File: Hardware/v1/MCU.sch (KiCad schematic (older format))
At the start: 63 parts, among them J10 SERV_0, J11 SERV_1, J12 SERV_2, J13 SERV_3, J14 SERV_0, J15 SERV_1, J16 SERV_2, J17 SERV_3, J18 GPIO1, J19 GPIO2, J20 GPIO3, J21 GPIO4, J22 GPIO5, J23 GPIO6, J24 DACS, J4 SERV_0, J5 SERV_1, J6 SERV_2, J7 SERV_3, J8 CAN, J9 USB_B_Mini, P1 SWD, SW2 BOOT0, U4 BMI160, U5 STM32F405RGTx, U6 TJA1051TK-3, Y1 8Mhz

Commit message: bah
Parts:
- J15: renamed from J10; value SERV_0 -> SERV_4
- J16: renamed from J11; value SERV_1 -> SERV_5
- J17: renamed from J12; value SERV_2 -> SERV_6
- J18: renamed from J13; value SERV_3 -> SERV_7
- J21: renamed from J14; value SERV_0 -> SERV_8
- J22: renamed from J15; value SERV_1 -> SERV_9
- J23: renamed from J16; value SERV_2 -> SERV_10
- J24: renamed from J17; value SERV_3 -> SERV_11
- renumbered C30 to C29, C31 to C30, C32 to C31, C33 to C32, C34 to C33, C35 to C34, J24 to J10, J4 to J11, J5 to J12, J6 to J13, J7 to J14, J8 to J19, J9 to J20, J18 to J4, J19 to J5, J20 to J6, J21 to J7, J22 to J8, J23 to J9, R12 to R11, R13 to R12, R15 to R13, R11 to R14, R14 to R15, R20 to R18, R21 to R19, R22 to R20, R23 to R21, R18 to R22, R24 to R23, R25 to R24, R26 to R25, R27 to R26, R19 to R27
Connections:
- net GND: no longer C28.2, J11.2 (Pin_2), J12.2 (Pin_2), J13.2 (Pin_2), J14.2 (Pin_2), J15.2 (Pin_2), J16.2 (Pin_2), J17.2 (Pin_2), J18.2 (Pin_2), J19.4 (Pin_4), J21.2 (Pin_2), J22.2 (Pin_2), J23.2 (Pin_2), J24.2 (Pin_2), U5.42 (PA9), U6.3 (VCC)
- new net +5V: C28.2, J11.2 (Pin_2), J12.2 (Pin_2), J13.2 (Pin_2), J14.2 (Pin_2), J15.2 (Pin_2), J16.2 (Pin_2), J17.2 (Pin_2), J18.2 (Pin_2), J19.4 (Pin_4), J21.2 (Pin_2), J22.2 (Pin_2), J23.2 (Pin_2), J24.2 (Pin_2), U5.42 (PA9), U6.3 (VCC)

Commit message: tweaks and simplification
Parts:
- removed J21: SERV_8, Connector_PinHeader_2.54mm:PinHeader_1x03_P2.54mm_Vertical, symbol Connector:Conn_01x03_Male
- removed J22: SERV_9, Connector_PinHeader_2.54mm:PinHeader_1x03_P2.54mm_Vertical, symbol Connector:Conn_01x03_Male
- removed J23: SERV_10, Connector_PinHeader_2.54mm:PinHeader_1x03_P2.54mm_Vertical, symbol Connector:Conn_01x03_Male
- removed J24: SERV_11, Connector_PinHeader_2.54mm:PinHeader_1x03_P2.54mm_Vertical, symbol Connector:Conn_01x03_Male
- removed J7: GPIO4, Connector_JST:JST_PH_B4B-PH-K_1x04_P2.00mm_Vertical, symbol Connector:Conn_01x04_Female
- removed J8: GPIO5, Connector_JST:JST_PH_B4B-PH-K_1x04_P2.00mm_Vertical, symbol Connector:Conn_01x04_Female
- removed J9: GPIO6, Connector_JST:JST_PH_B4B-PH-K_1x04_P2.00mm_Vertical, symbol Connector:Conn_01x04_Female
- removed R23, R24, R25, R26: 220R, Resistor_SMD:R_0603_1608Metric, symbol Device:R_Small
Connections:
- net GP14 is gone; now on net IMU_INT2: U5.25 (PC5)
- net IMU_INT2: no longer U5.57 (PB5)
- net GP10: no longer names the net of U5.33 (PB12)
- net GP11: no longer names the net of U5.34 (PB13)
- net GP12: no longer names the net of U5.35 (PB14)
- net GP13: no longer names the net of U5.24 (PC4)
- net GP15: no longer names the net of U5.4 (PC15)
- net GP16: no longer names the net of U5.58 (PB6)
- net GP17: no longer names the net of U5.59 (PB7)
- net GP18: no longer names the net of U5.36 (PB15)
- net SERV10: no longer names the net of U5.38 (PC7)
- net SERV11: no longer names the net of U5.39 (PC8)
- net SERV12: no longer names the net of U5.40 (PC9)
- net SERV9: no longer names the net of U5.37 (PC6)
- no-connect marks 10 -> 23

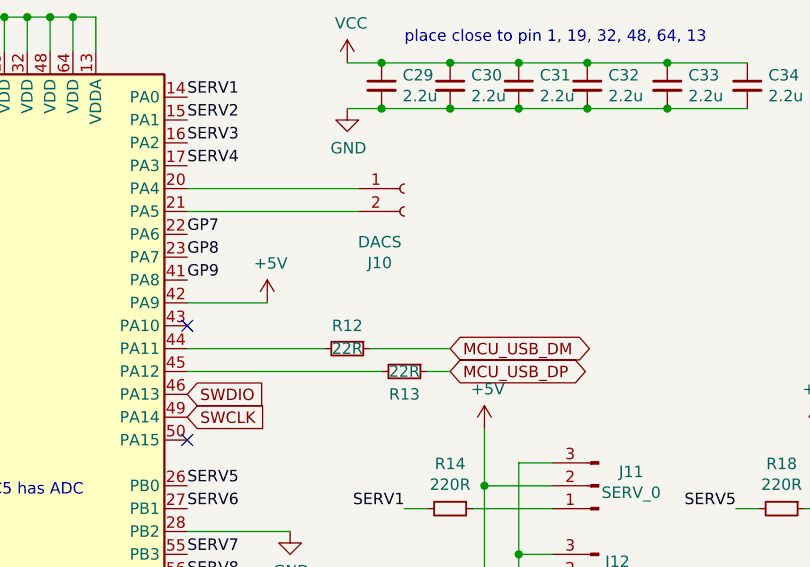
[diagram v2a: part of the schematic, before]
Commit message: adding some descriptions on F silks
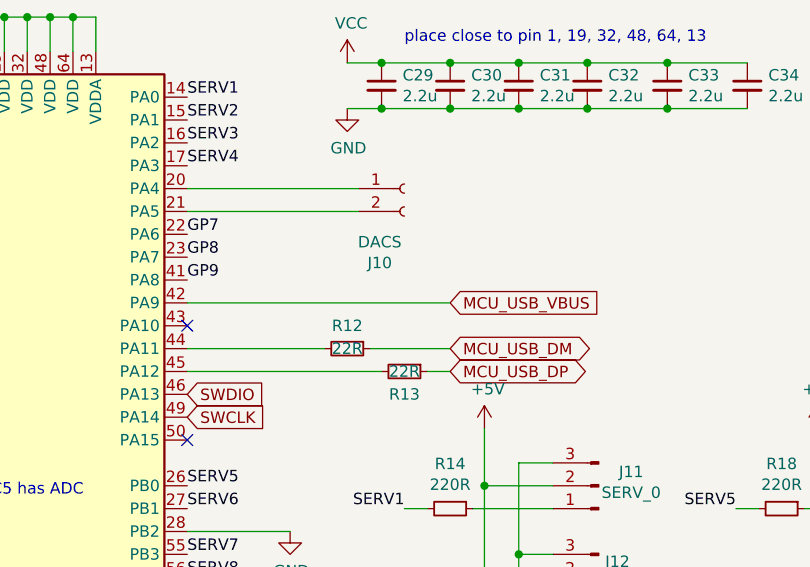
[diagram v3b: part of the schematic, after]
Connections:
- net +5V: no longer U5.42 (PA9)
- net MCU_USB_VBUS: now also U5.42 (PA9)
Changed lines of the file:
@@
 LED1
-Wire Wire Line
-	5750 2700 6100 2700
-$Comp
-L Device:R_Small R12
-U 1 1 5D93C493
-P 5650 2700
-F 0 "R12" V 5550 2700 50  0000 C CNN
-F 1 "22R" V 5650 2700 50  0000 C CNN
-F 2 "Resistor_SMD:R_0603_1608Metric" H 5650 2700 50  0001 C CNN
-F 3 "~" H 5650 2700 50  0001 C CNN
-F 4 "311-22GRCT-ND" H 5650 2700 50  0001 C CNN "OrderN"
-	1    5650 2700
-	0    1    1    0
-$EndComp
 Wire Wire Line
 	4950 2800 5800 2800
@@
 	-1   0    0    1
 $EndComp
-Wire Wire Line
-	4950 2700 5550 2700
 Wire Wire Line
 	9800 2200 10500 2200
@@
 	4900 5950 5600 5950
 $Comp
-L power:+5V #PWR034
-U 1 1 5E17915F
-P 5300 2500
-F 0 "#PWR034" H 5300 2350 50  0001 C CNN
-F 1 "+5V" H 5315 2673 50  0000 C CNN
-F 2 "" H 5300 2500 50  0001 C CNN
-F 3 "" H 5300 2500 50  0001 C CNN
-	1    5300 2500
-	1    0    0    -1
-$EndComp
-Wire Wire Line
-	4950 2500 5300 2500
-$Comp
 L power:+5V #PWR0101
 U 1 1 5E0CAA07
@@
 SDA
 NoConn ~ 4950 3800
+Text GLabel 6100 2500 2    50   Input ~ 0
+MCU_USB_VBUS
+Wire Wire Line
+	4950 2700 5550 2700
+Wire Wire Line
+	5750 2700 6100 2700
+$Comp
+L Device:R_Small R12
+U 1 1 5D93C493
+P 5650 2700
+F 0 "R12" V 5550 2700 50  0000 C CNN
+F 1 "22R" V 5650 2700 50  0000 C CNN
+F 2 "Resistor_SMD:R_0603_1608Metric" H 5650 2700 50  0001 C CNN
+F 3 "~" H 5650 2700 50  0001 C CNN
+F 4 "311-22GRCT-ND" H 5650 2700 50  0001 C CNN "OrderN"
+	1    5650 2700
+	0    1    1    0
+$EndComp
+Wire Wire Line
+	4950 2500 6100 2500
 $EndSCHEMATC
